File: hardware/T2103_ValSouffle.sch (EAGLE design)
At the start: 42 parts, among them IC1 LM317MB, Q1 IRFB4310ZPBF, T1 2N2222, U1 ATMEGA328P-PU, U2 SN74HC595N, X1 16Mhz

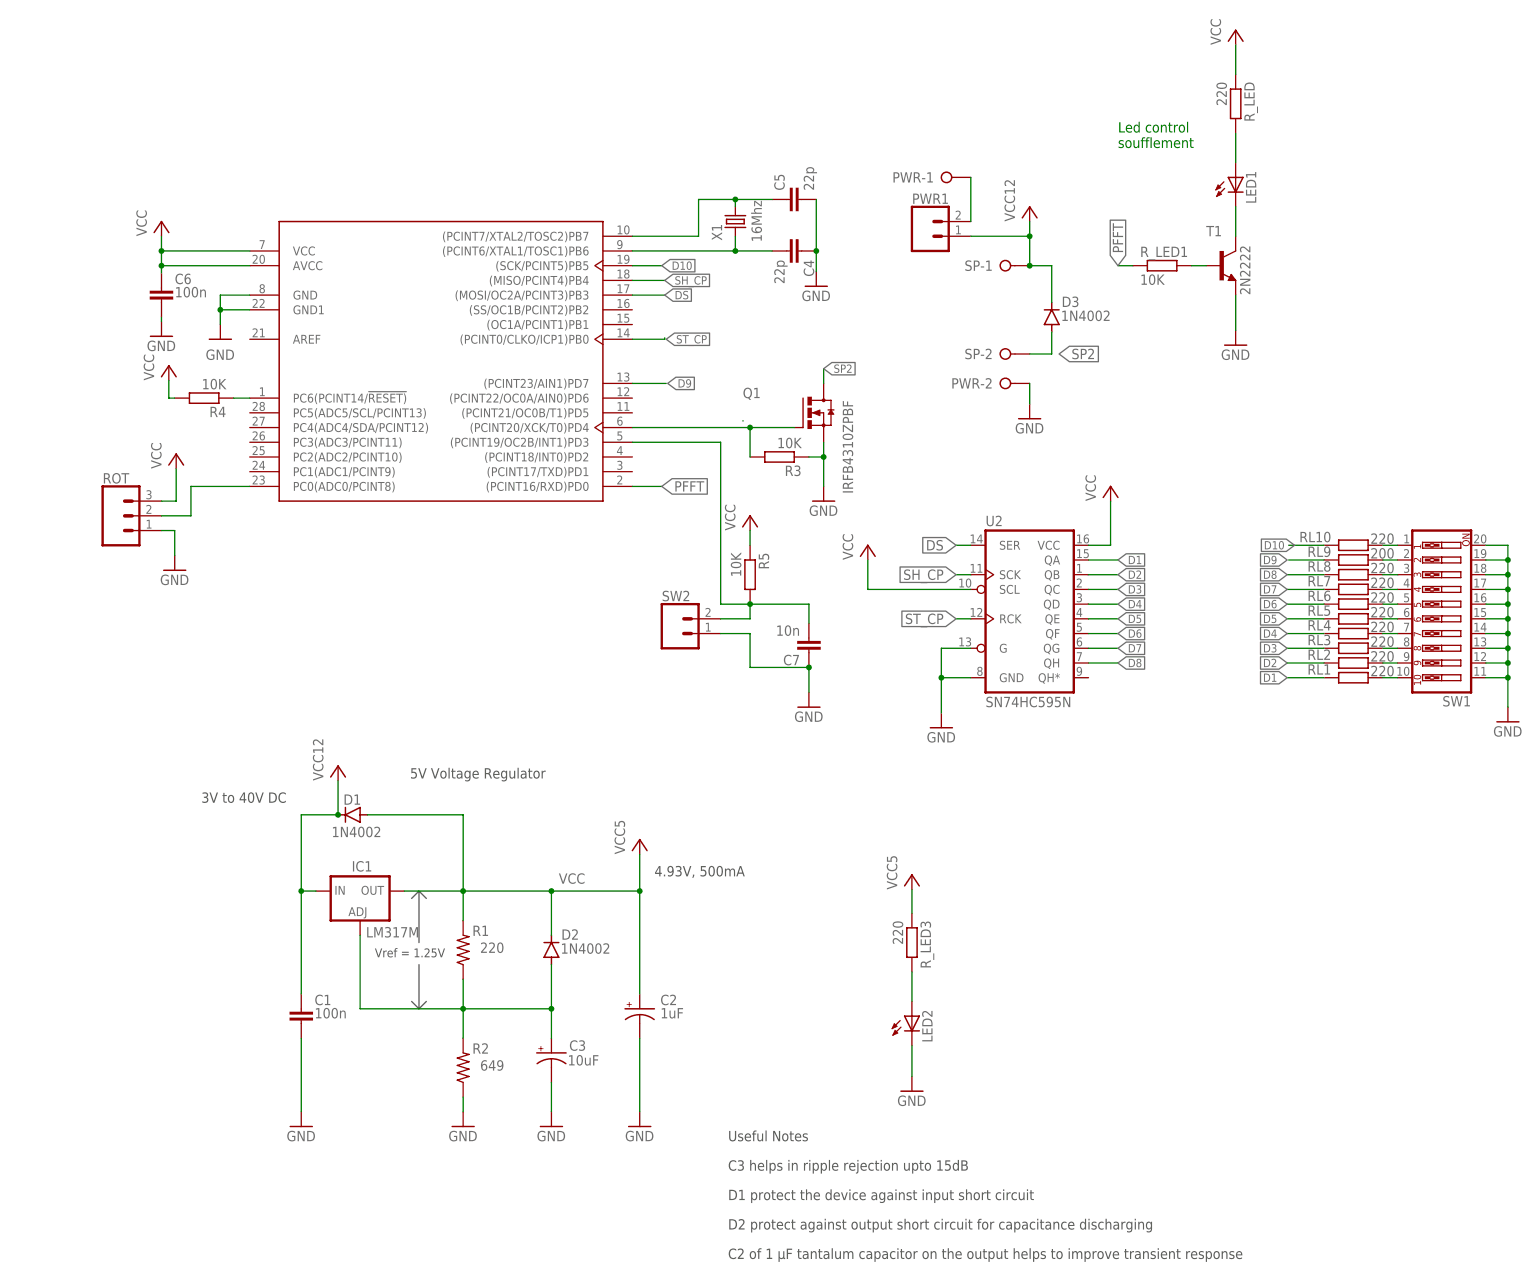
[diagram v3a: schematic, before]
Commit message: update graph
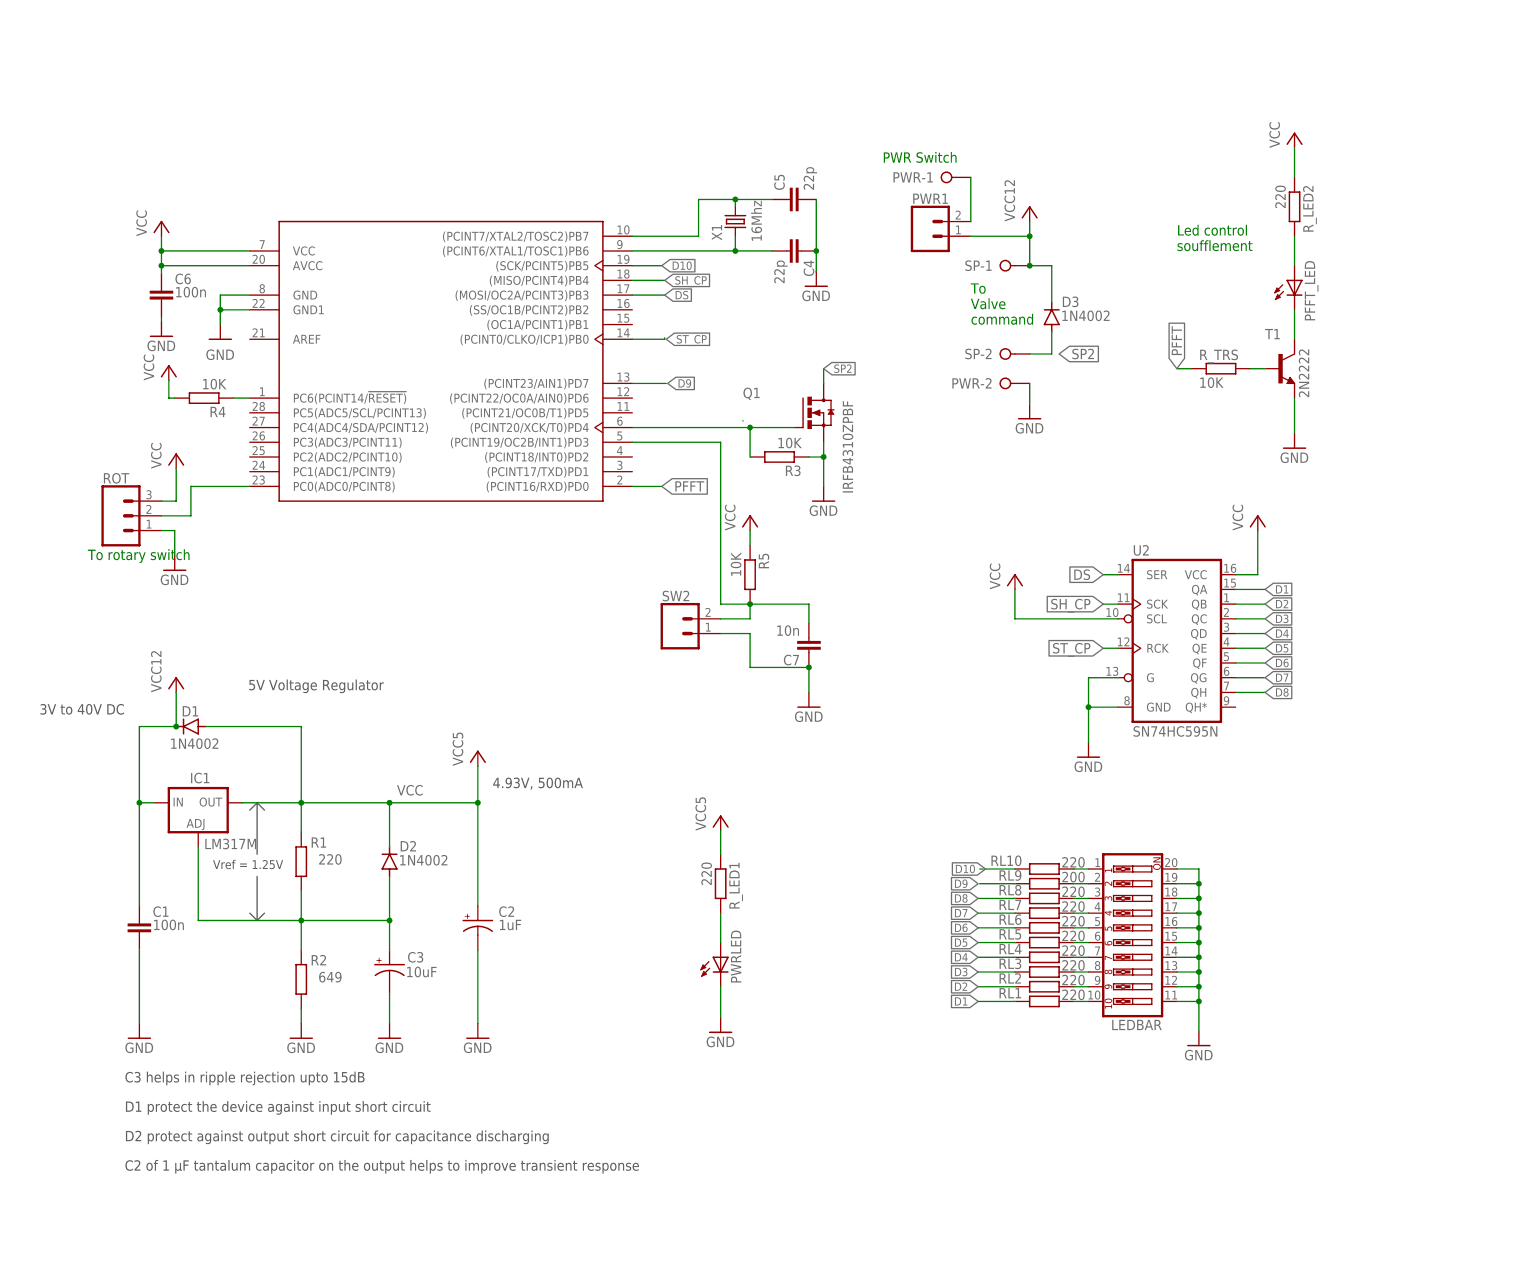
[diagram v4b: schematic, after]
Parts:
- removed LED1, LED2: (no value), adafruit:LED5MM
- removed R_LED, R_LED3: 220, resistor:R-EU_0207/10
- removed SW1: (no value), special:SW_DIP-10
- added LEDBAR: (no value), special:SW_DIP-10
- added PFFT_LED, PWRLED: (no value), adafruit:LED5MM
- added R_LED2: 220, resistor:R-EU_0207/10
- added R_TRS: 10K, resistor:R-EU_0207/10
- R1, R2: device resistor:R-US_0207/10 -> rcl:R-EU_0207/10
- R_LED1: value 10K -> 220
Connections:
- net GND: now also LEDBAR.11, LEDBAR.12, LEDBAR.13, LEDBAR.14, LEDBAR.15, LEDBAR.16, LEDBAR.17, LEDBAR.18, LEDBAR.19, LEDBAR.20, PWRLED.C; no longer LED2.C, SW1.11, SW1.12, SW1.13, SW1.14, SW1.15, SW1.16, SW1.17, SW1.18, SW1.19, SW1.20
- net N$10: now also LEDBAR.5; no longer SW1.5
- net N$11: now also LEDBAR.6; no longer SW1.6
- net N$12: now also LEDBAR.7; no longer SW1.7
- net N$13: now also LEDBAR.8; no longer SW1.8
- net N$14: now also LEDBAR.9; no longer SW1.9
- net N$15: now also LEDBAR.10; no longer SW1.10
- net N$18: now also PFFT_LED.A, R_LED2.2; no longer LED1.A, R_LED.2
- net N$19: now also PFFT_LED.C; no longer LED1.C
- net N$20: now also PWRLED.A, R_LED1.2; no longer LED2.A, R_LED3.2
- net N$21: now also R_TRS.2; no longer R_LED1.2
- net N$6: now also LEDBAR.1; no longer SW1.1
- net N$7: now also LEDBAR.2; no longer SW1.2
- net N$8: now also LEDBAR.3; no longer SW1.3
- net N$9: now also LEDBAR.4; no longer SW1.4
- net PFFT: now also R_TRS.1; no longer R_LED1.1
- net VCC: now also R_LED1.1, R_LED2.1; no longer R_LED.1, R_LED3.1
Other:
- note added: "PWR Switch"
- note added: "To Valve command"
- note added: "To rotary switch"
- note removed: "Useful Notes"
- moved on the sheet: C1, C2, C3, D1, D2, IC1, RL1, RL10, RL2, RL3, RL4, RL5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
